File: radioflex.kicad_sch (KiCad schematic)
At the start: 2 parts, among them CN18 DF40C-20DS-0.4V, CN19 DF40C-20DS-0.4V

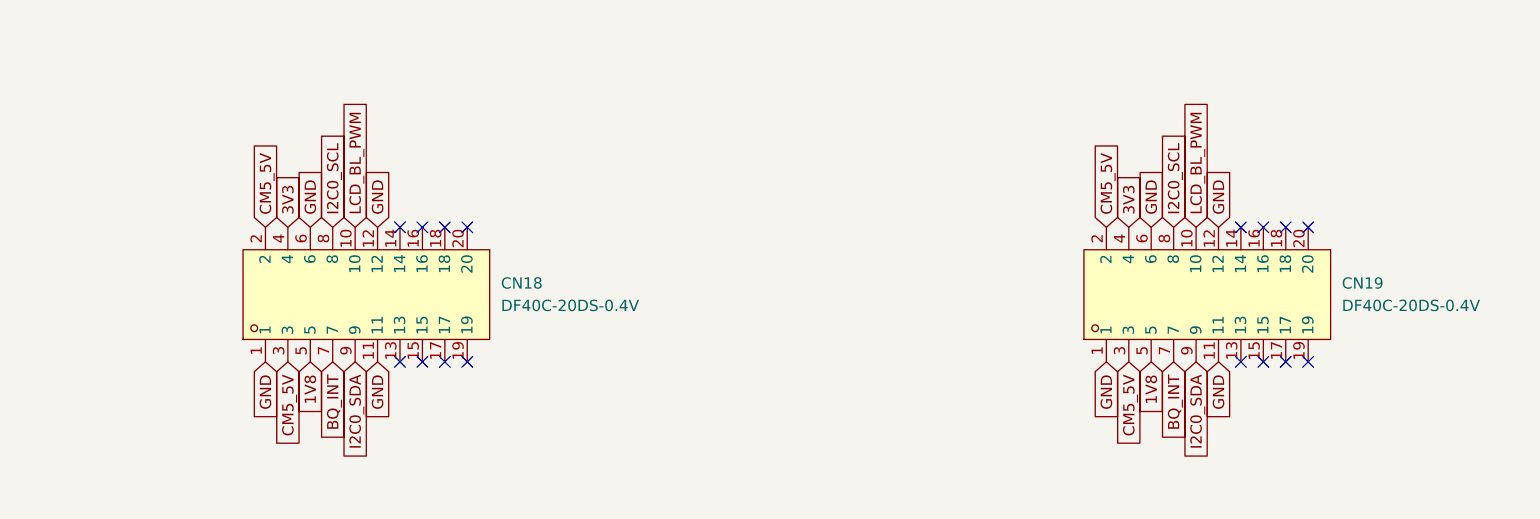
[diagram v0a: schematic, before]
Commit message: finished radio board with load switches and flash, fixed b2b connector, started antenna module and rf sense switching circuit
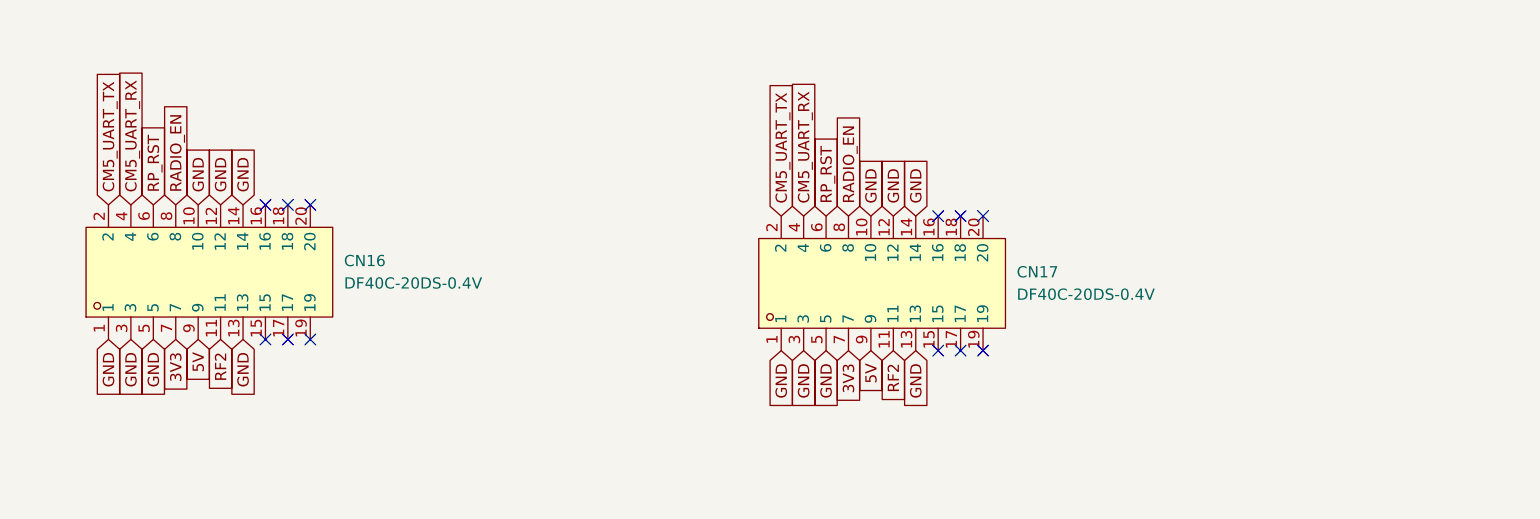
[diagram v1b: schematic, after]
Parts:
- removed CN18, CN19: DF40C-20DS-0.4V, slate113:CONN-SMD_20P-P0.40_DF40C-20DS-0.4V, symbol slate113:DF40C-20DS-0.4V
- added CN16, CN17: DF40C-20DS-0.4V, slate113:CONN-SMD_20P-P0.40_DF40C-20DS-0.4V, symbol slate113:DF40C-20DS-0.4V
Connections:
- net 3V3: now also CN16.7, CN17.7
- net GND: now also CN16.1, CN16.10, CN16.12, CN16.13, CN16.14, CN16.3, CN16.5, CN17.1, CN17.10, CN17.12, CN17.13, CN17.14, CN17.3, CN17.5
- new net 5V: CN16.9, CN17.9
- new net CM5_UART_RX: CN16.4, CN17.4
- new net CM5_UART_TX: CN16.2, CN17.2
- new net RADIO_EN: CN16.8, CN17.8
- new net RF2: CN16.11, CN17.11
- new net RP_RST: CN16.6, CN17.6
- no-connect marks 16 -> 12

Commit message: finished slateconnect i2c gpio expander, completed led status bar schematic, fixed all drc errors, started assigning footprints and started bom
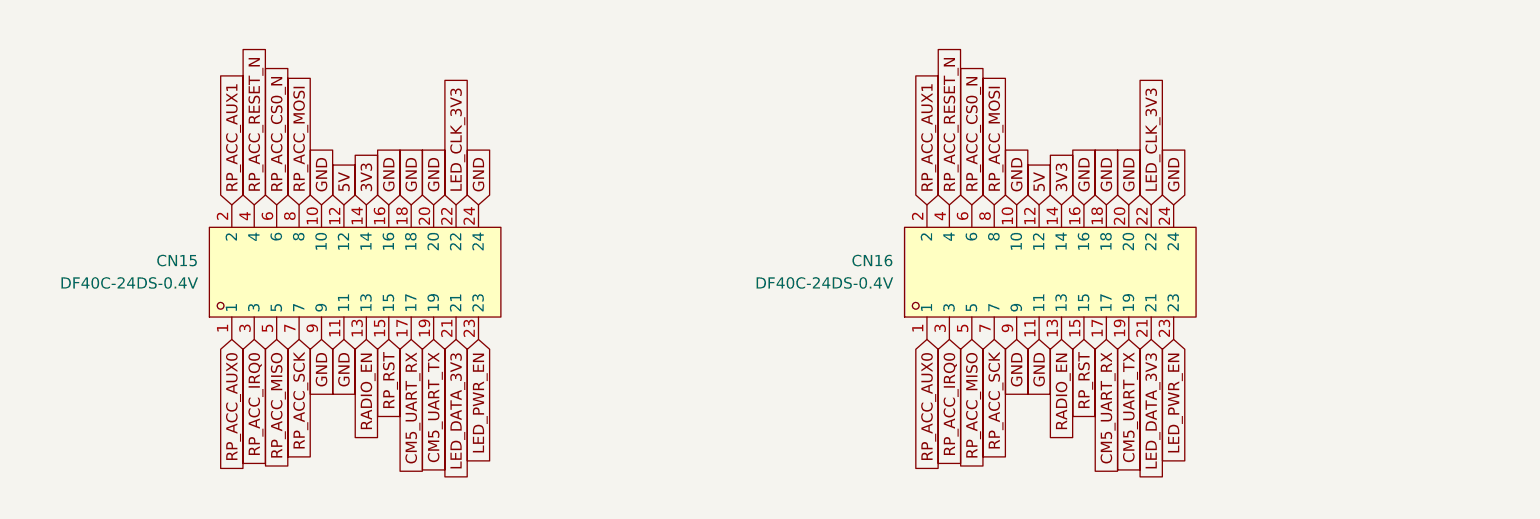
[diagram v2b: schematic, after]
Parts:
- removed CN16, CN17: DF40C-20DS-0.4V, slate113:CONN-SMD_20P-P0.40_DF40C-20DS-0.4V, symbol slate113:DF40C-20DS-0.4V
- added CN15, CN16: DF40C-24DS-0.4V, slate113:CONN-SMD_DF40C-24DS-0.4V51, symbol slate113:DF40C-24DS-0.4V
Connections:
- net 3V3: now also CN15.14, CN16.14
- net 5V: now also CN15.12, CN16.12
- net CM5_UART_RX: now also CN15.17, CN16.17
- net CM5_UART_TX: now also CN15.19, CN16.19
- net GND: now also CN15.10, CN15.11, CN15.16, CN15.18, CN15.20, CN15.24, CN15.9, CN16.10, CN16.11, CN16.16, CN16.18, CN16.20, CN16.24, CN16.9
- net RADIO_EN: now also CN15.13, CN16.13
- net RP_RST: now also CN15.15, CN16.15
- new net LED_CLK_3V3: CN15.22, CN16.22
- new net LED_DATA_3V3: CN15.21, CN16.21
- new net LED_PWR_EN: CN15.23, CN16.23
- new net RP_ACC_AUX0: CN15.1, CN16.1
- new net RP_ACC_AUX1: CN15.2, CN16.2
- new net RP_ACC_CS0_N: CN15.6, CN16.6
- new net RP_ACC_IRQ0: CN15.3, CN16.3
- new net RP_ACC_MISO: CN15.5, CN16.5
- new net RP_ACC_MOSI: CN15.8, CN16.8
- new net RP_ACC_RESET_N: CN15.4, CN16.4
- new net RP_ACC_SCK: CN15.7, CN16.7
- no-connect marks 12 -> 0

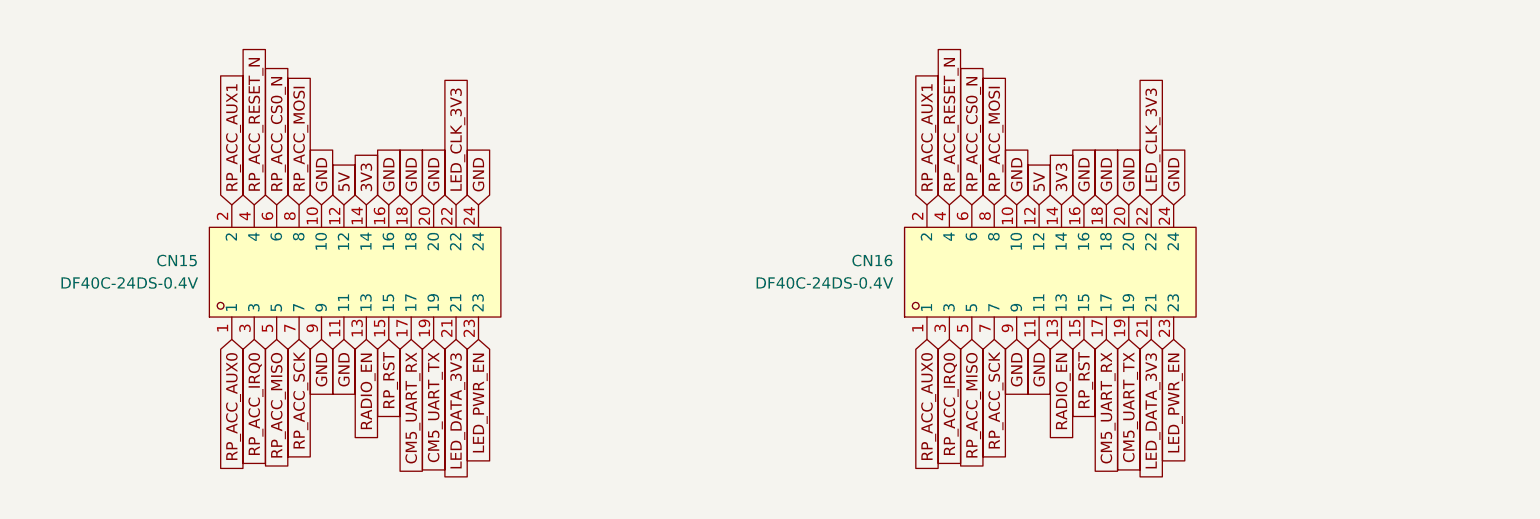
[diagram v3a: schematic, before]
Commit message: imported footprints and 3d models, replaced obsolete components, finished schematic audit, wired new usb hub and flash chip + more, removed stale nets
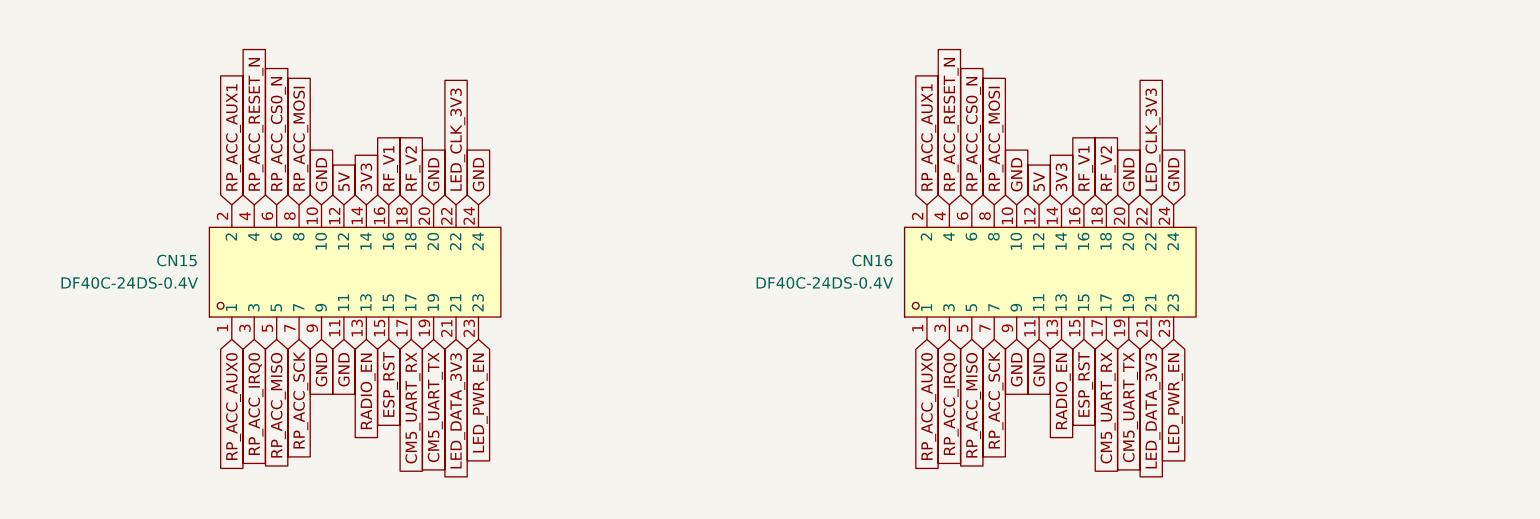
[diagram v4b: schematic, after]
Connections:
- net GND: no longer CN15.16, CN15.18, CN16.16, CN16.18
- net RP_RST renamed ESP_RST
- new net RF_V1: CN15.16, CN16.16
- new net RF_V2: CN15.18, CN16.18
